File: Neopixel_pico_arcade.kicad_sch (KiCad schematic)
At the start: 19 parts, among them J1 SWD_connector, J2 NES_controller_connector, J3 USB_C_Receptacle_USB2.0, Q1 2N7002, U1 RP2040_Stamp, U2 SN74LV1T34DBV, U3 SRV05-4HTG-D

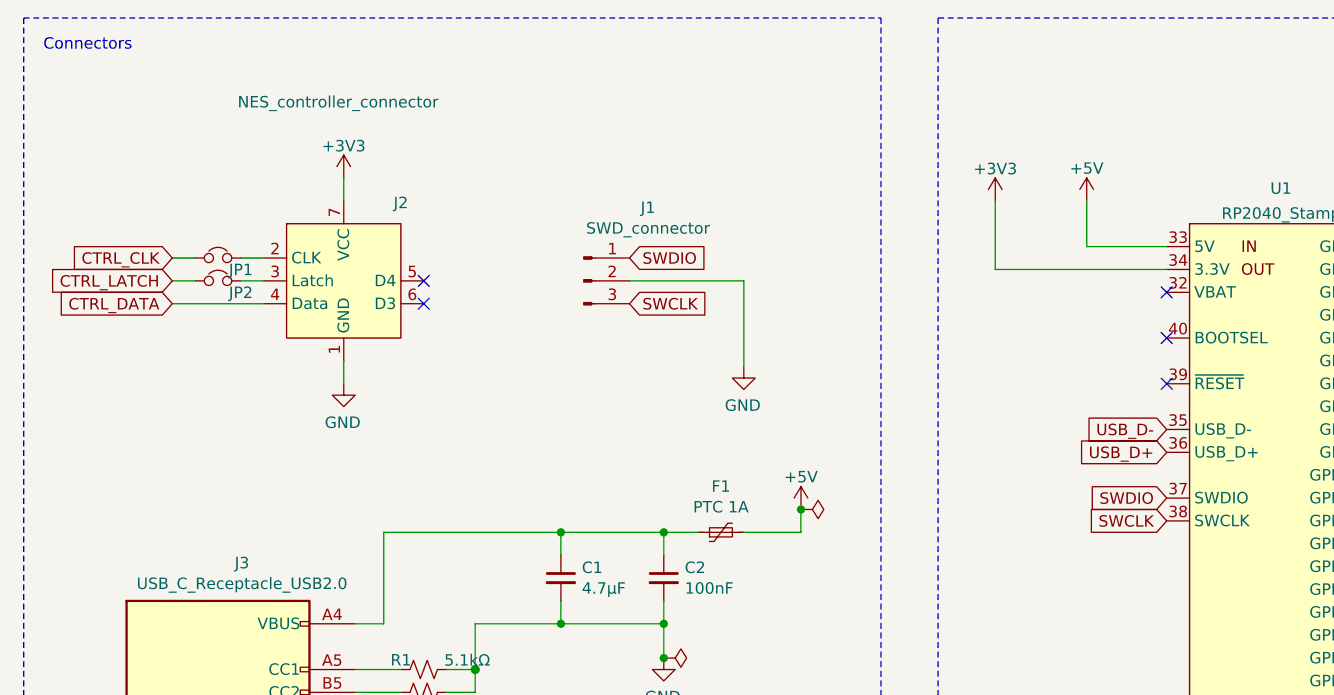
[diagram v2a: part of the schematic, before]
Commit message: Removes SWD header
We will very likely not need it anyways since we have a USB connection
for programming.
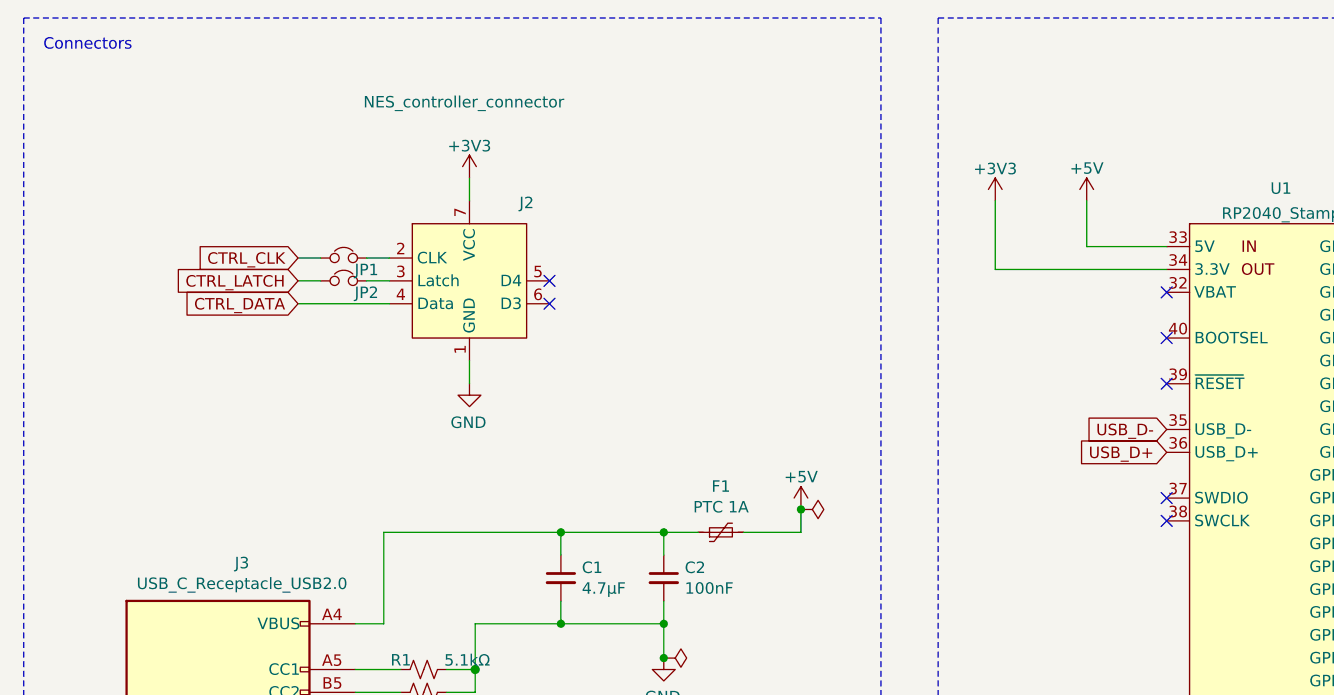
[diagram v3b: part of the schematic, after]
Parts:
- removed J1: SWD_connector, Connector_PinHeader_2.54mm:PinHeader_1x03_P2.54mm_Vertical_SMD_Pin1Left, symbol Connector:Conn_01x03_Male
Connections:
- net SWCLK: no longer names the net of U1.38 (SWCLK)
- net SWDIO: no longer names the net of U1.37 (SWDIO)
- no-connect marks 34 -> 36
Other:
- moved on the sheet: J2, JP1, JP2

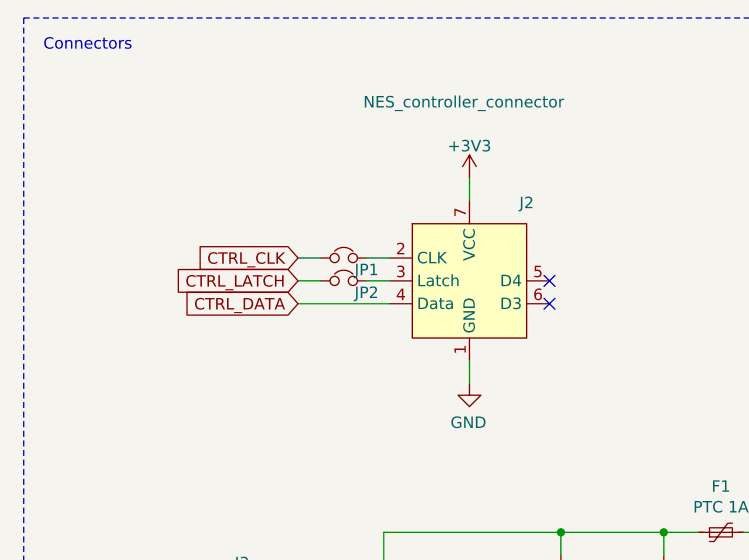
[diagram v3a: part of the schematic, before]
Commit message: Removes jumpers from schematics
If we mix up clock and latch we can swap them in software
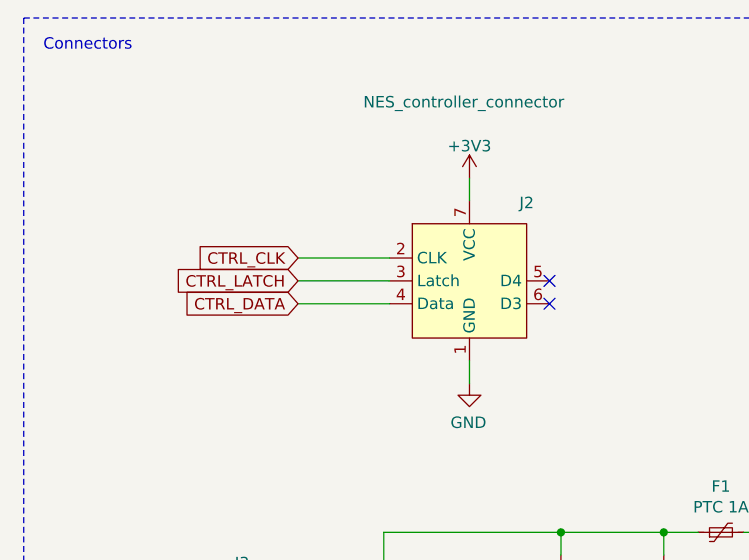
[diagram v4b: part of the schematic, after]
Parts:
- removed JP1, JP2: jmp, Jumper:SolderJumper-2_P1.3mm_Bridged_RoundedPad1.0x1.5mm, symbol Device:Jumper_NC_Small
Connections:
- net CTRL_CLK: now also J2.2 (CLK)
- net CTRL_LATCH: now also J2.3 (Latch)
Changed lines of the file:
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@@
     (stroke (width 0) (type default) (color 0 0 0 0))
   )
-  (wire (pts (xy 49.53 44.45) (xy 52.07 44.45))
-    (stroke (width 0) (type default) (color 0 0 0 0))
-  )
-  (wire (pts (xy 49.53 46.99) (xy 52.07 46.99))
+  (wire (pts (xy 49.53 44.45) (xy 59.69 44.45))
+    (stroke (width 0) (type default) (color 0 0 0 0))
+  )
+  (wire (pts (xy 49.53 46.99) (xy 59.69 46.99))
     (stroke (width 0) (type default) (color 0 0 0 0))
   )
@@
   (wire (pts (xy 55.88 105.41) (xy 57.15 105.41))
     (stroke (width 0) (type solid) (color 0 0 0 0))
-  )
-  (wire (pts (xy 57.15 44.45) (xy 59.69 44.45))
-    (stroke (width 0) (type default) (color 0 0 0 0))
-  )
-  (wire (pts (xy 57.15 46.99) (xy 59.69 46.99))
-    (stroke (width 0) (type default) (color 0 0 0 0))
   )
   (wire (pts (xy 57.15 97.79) (xy 57.15 100.33))
@@
     )
     (pin "1")
-  )
-  (symbol (lib_id "Device:Jumper_NC_Small") (at 54.61 44.45 0) (unit 1)
-    (in_bom yes) (on_board yes)
-    (property "Reference" "JP1" (id 0) (at 57.15 45.7666 0))
-    (property "Value" "jmp" (id 1) (at 50.8 47.2717 0)
-      (effects (font (size 1.27 1.27)) hide)
-    )
-    (property "Footprint" "Jumper:SolderJumper-2_P1.3mm_Bridged_RoundedPad1.0x1.5mm" (id 2) (at 54.61 44.45 0)
-      (effects (font (size 1.27 1.27)) hide)
-    )
-    (property "Datasheet" "~" (id 3) (at 54.61 44.45 0)
-      (effects (font (size 1.27 1.27)) hide)
-    )
-    (pin "1")
-    (pin "2")
-  )
-  (symbol (lib_id "Device:Jumper_NC_Small") (at 54.61 46.99 0) (unit 1)
-    (in_bom yes) (on_board yes)
-    (property "Reference" "JP2" (id 0) (at 57.15 48.3066 0))
-    (property "Value" "jmp" (id 1) (at 54.61 48.5417 0)
-      (effects (font (size 1.27 1.27)) hide)
-    )
-    (property "Footprint" "Jumper:SolderJumper-2_P1.3mm_Bridged_RoundedPad1.0x1.5mm" (id 2) (at 54.61 46.99 0)
-      (effects (font (size 1.27 1.27)) hide)
-    )
-    (property "Datasheet" "~" (id 3) (at 54.61 46.99 0)
-      (effects (font (size 1.27 1.27)) hide)
-    )
-    (pin "1")
-    (pin "2")
   )
   (symbol (lib_id "Device:R_Small_US") (at 63.5 90.17 90) (unit 1)
@@
       (reference "J3") (unit 1) (value "USB_C_Receptacle_USB2.0") (footprint "Neopixel_pico_arcade:USB_C_Receptacle_USB_2_GTC_USB4105")
     )
-    (path "/a9c99e6b-55b1-4adc-8611-0aea35c1c656"
-      (reference "JP1") (unit 1) (value "jmp") (footprint "Jumper:SolderJumper-2_P1.3mm_Bridged_RoundedPad1.0x1.5mm")
-    )
-    (path "/87921a4f-6ae8-4267-b5e7-44fa4718debc"
-      (reference "JP2") (unit 1) (value "jmp") (footprint "Jumper:SolderJumper-2_P1.3mm_Bridged_RoundedPad1.0x1.5mm")
-    )
     (path "/691f88c6-2cd2-4539-9dfe-b9f1bc68fc22"
